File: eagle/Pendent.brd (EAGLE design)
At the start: 40.6 x 40.6 mm, 38 parts, among them Q1 CMA-4544PF-W, Q2 MPSA42, Q3 8/16/20MHz, U1 MAX9814TDFN14, U2 LF50ABDT-TR, U3 ATMEGA328

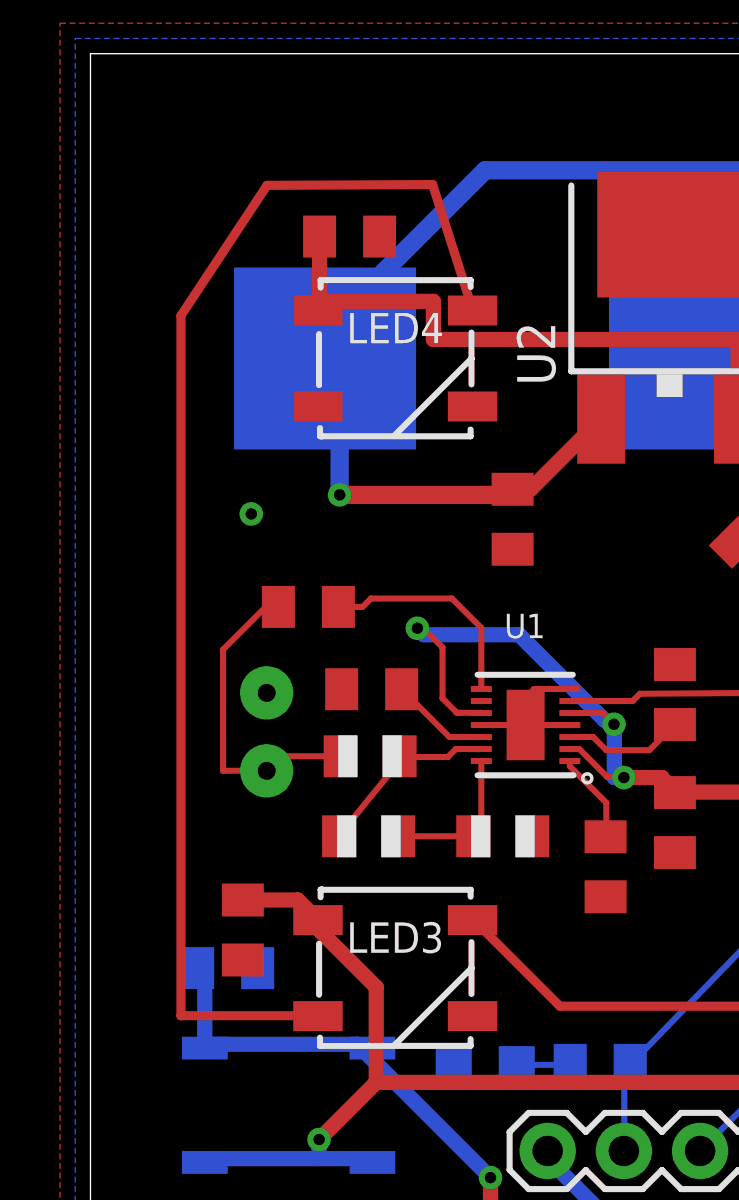
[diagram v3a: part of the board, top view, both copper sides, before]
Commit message: Add External LED Connection
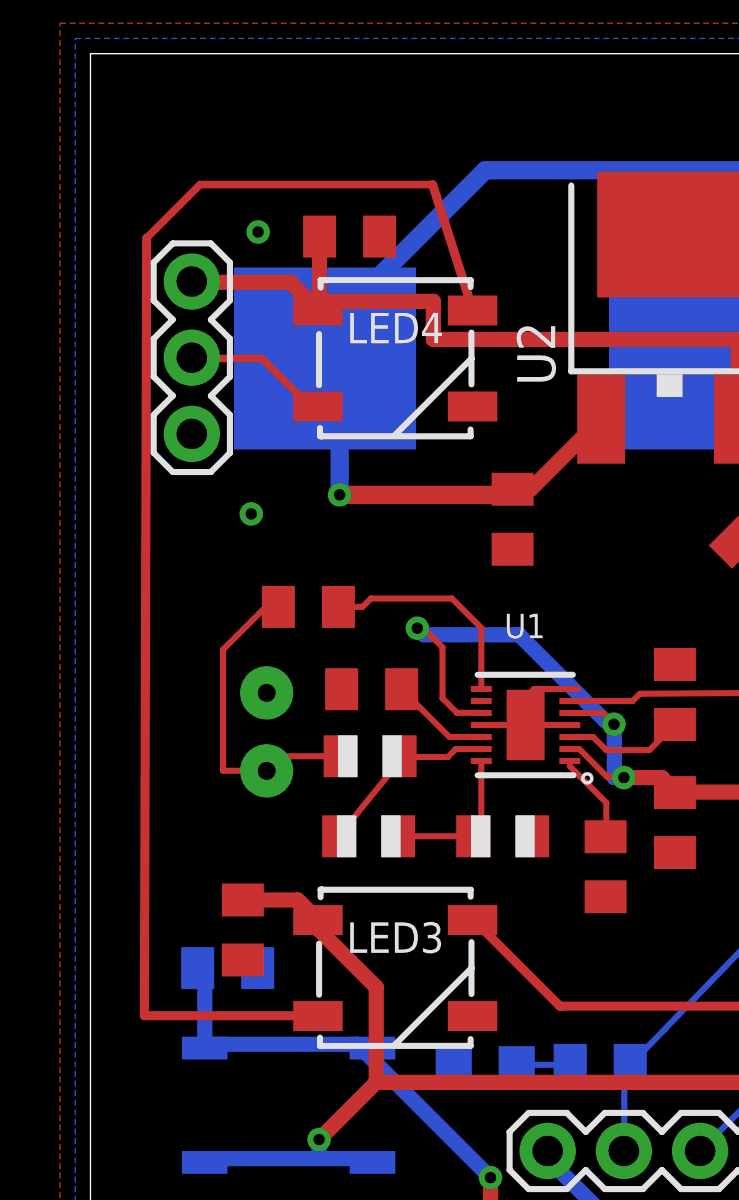
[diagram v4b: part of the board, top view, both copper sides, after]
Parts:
- added JP1: (no value), SparkFun-Connectors:1X03
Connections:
- new net N$6: JP1.2, LED4.2
- net GND: now also JP1.1
- net VCC: now also JP1.3
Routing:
- net N$6: track 0.00 -> 4.87 mm
- net VCC: track 175.1 -> 179.7 mm
- net N$3: track 43.0 -> 46.4 mm
- net GND: vias 5 -> 6
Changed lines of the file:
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@@
 <grid distance="0.1" unitdist="inch" unit="inch" style="lines" multiple="1" display="yes" altdistance="0.001" altunitdist="inch" altunit="inch"/>
 <layers>
-<layer number="1" name="Top" color="4" fill="1" visible="no" active="yes"/>
-<layer number="16" name="Bottom" color="1" fill="1" visible="no" active="yes"/>
+<layer number="1" name="Top" color="4" fill="1" visible="yes" active="yes"/>
+<layer number="16" name="Bottom" color="1" fill="1" visible="yes" active="yes"/>
 <layer number="17" name="Pads" color="2" fill="1" visible="yes" active="yes"/>
 <layer number="18" name="Vias" color="2" fill="1" visible="yes" active="yes"/>
@@
 <layer number="20" name="Dimension" color="15" fill="1" visible="yes" active="yes"/>
 <layer number="21" name="tPlace" color="7" fill="1" visible="yes" active="yes"/>
-<layer number="22" name="bPlace" color="7" fill="1" visible="no" active="yes"/>
+<layer number="22" name="bPlace" color="7" fill="1" visible="yes" active="yes"/>
 <layer number="23" name="tOrigins" color="15" fill="1" visible="yes" active="yes"/>
-<layer number="24" name="bOrigins" color="15" fill="1" visible="no" active="yes"/>
+<layer number="24" name="bOrigins" color="15" fill="1" visible="yes" active="yes"/>
 <layer number="25" name="tNames" color="7" fill="1" visible="yes" active="yes"/>
-<layer number="26" name="bNames" color="7" fill="1" visible="no" active="yes"/>
+<layer number="26" name="bNames" color="7" fill="1" visible="yes" active="yes"/>
 <layer number="27" name="tValues" color="7" fill="1" visible="yes" active="yes"/>
-<layer number="28" name="bValues" color="7" fill="1" visible="no" active="yes"/>
+<layer number="28" name="bValues" color="7" fill="1" visible="yes" active="yes"/>
 <layer number="29" name="tStop" color="7" fill="3" visible="yes" active="yes"/>
-<layer number="30" name="bStop" color="7" fill="6" visible="no" active="yes"/>
+<layer number="30" name="bStop" color="7" fill="6" visible="yes" active="yes"/>
 <layer number="31" name="tCream" color="7" fill="4" visible="yes" active="yes"/>
-<layer number="32" name="bCream" color="7" fill="5" visible="no" active="yes"/>
+<layer number="32" name="bCream" color="7" fill="5" visible="yes" active="yes"/>
 <layer number="33" name="tFinish" color="6" fill="3" visible="yes" active="yes"/>
-<layer number="34" name="bFinish" color="6" fill="6" visible="no" active="yes"/>
+<layer number="34" name="bFinish" color="6" fill="6" visible="yes" active="yes"/>
 <layer number="35" name="tGlue" color="7" fill="4" visible="yes" active="yes"/>
-<layer number="36" name="bGlue" color="7" fill="5" visible="no" active="yes"/>
+<layer number="36" name="bGlue" color="7" fill="5" visible="yes" active="yes"/>
 <layer number="37" name="tTest" color="7" fill="1" visible="yes" active="yes"/>
-<layer number="38" name="bTest" color="7" fill="1" visible="no" active="yes"/>
+<layer number="38" name="bTest" color="7" fill="1" visible="yes" active="yes"/>
 <layer number="39" name="tKeepout" color="4" fill="11" visible="yes" active="yes"/>
-<layer number="40" name="bKeepout" color="1" fill="11" visible="no" active="yes"/>
+<layer number="40" name="bKeepout" color="1" fill="11" visible="yes" active="yes"/>
 <layer number="41" name="tRestrict" color="4" fill="10" visible="yes" active="yes"/>
-<layer number="42" name="bRestrict" color="1" fill="10" visible="no" active="yes"/>
-<layer number="43" name="vRestrict" color="2" fill="10" visible="no" active="yes"/>
+<layer number="42" name="bRestrict" color="1" fill="10" visible="yes" active="yes"/>
+<layer number="43" name="vRestrict" color="2" fill="10" visible="yes" active="yes"/>
 <layer number="44" name="Drills" color="7" fill="1" visible="yes" active="yes"/>
 <layer number="45" name="Holes" color="7" fill="1" visible="yes" active="yes"/>
@@
 <layer number="49" name="Reference" color="7" fill="1" visible="yes" active="yes"/>
 <layer number="50" name="dxf" color="7" fill="1" visible="no" active="no"/>
-<layer number="51" name="tDocu" color="7" fill="1" visible="no" active="yes"/>
+<layer number="51" name="tDocu" color="7" fill="1" visible="yes" active="yes"/>
 <layer number="52" name="bDocu" color="7" fill="1" visible="yes" active="yes"/>
 <layer number="53" name="tGND_GNDA" color="7" fill="9" visible="no" active="no"/>
@@
 <text x="24.1554" y="1.4224" size="0.8128" layer="27">GND</text>
 <text x="29.0576" y="22.7838" size="0.8128" layer="52" rot="MR135">RESET</text>
+<text x="1.8542" y="26.8478" size="0.762" layer="27" rot="R90">GND</text>
 </plain>
 <attributes>
@@
 <attribute name="VALUE" x="39.2811" y="14.1605" size="0.8128" layer="27" rot="R90"/>
 </element>
+<element name="JP1" library="SparkFun-Connectors" package="1X03" value="" x="3.3782" y="27.9654" smashed="yes" rot="R90">
+<attribute name="VALUE" x="6.5532" y="26.6954" size="1.27" layer="27" rot="R90"/>
+</element>
 </elements>
 <signals>
@@
 <contactref element="C9" pad="1"/>
 <contactref element="C5" pad="1"/>
-<contactref element="LED4" pad="1"/>
 <contactref element="C2" pad="1"/>
 <contactref element="LED1" pad="1"/>
@@
 <wire x1="6.913" y1="12.43" x2="7.583" y2="11.76" width="0.508" layer="1"/>
 <wire x1="7.636" y1="34.544" x2="7.636" y2="32.133" width="0.508" layer="1"/>
-<wire x1="7.636" y1="32.133" x2="7.583" y2="32.08" width="0.508" layer="1"/>
 <wire x1="27.956" y1="34.544" x2="27.956" y2="32.133" width="0.508" layer="1"/>
 <wire x1="27.956" y1="32.133" x2="27.903" y2="32.08" width="0.508" layer="1"/>
@@
 <wire x1="21.59" y1="31.115" x2="11.43" y2="31.115" width="0.508" layer="1"/>
 <wire x1="21.59" y1="28.575" x2="21.59" y2="31.115" width="0.508" layer="1"/>
-<wire x1="7.62" y1="32.385" x2="7.583" y2="32.08" width="0.508" layer="1"/>
 <wire x1="21.59" y1="28.575" x2="21.584" y2="28.472" width="0.508" layer="1"/>
 <wire x1="9.525" y1="9.525" x2="7.62" y2="11.43" width="0.508" layer="1"/>
@@
 <wire x1="32.812053125" y1="19.05" x2="31.75" y2="19.05" width="0.508" layer="1"/>
 <wire x1="31.75" y1="19.05" x2="31.115" y2="18.415" width="0.508" layer="1"/>
+<contactref element="LED4" pad="1"/>
+<contactref element="JP1" pad="3"/>
+<wire x1="7.62" y1="32.0675" x2="7.583" y2="32.08" width="0.508" layer="1"/>
+<wire x1="7.62" y1="32.0675" x2="7.636" y2="32.133" width="0.508" layer="1"/>
+<wire x1="7.62" y1="32.385" x2="7.583" y2="32.08" width="0.508" layer="1"/>
+<wire x1="6.6675" y1="33.02" x2="7.3025" y2="32.385" width="0.508" layer="1"/>
+<wire x1="3.4925" y1="33.02" x2="6.6675" y2="33.02" width="0.508" layer="1"/>
+<wire x1="7.3025" y1="32.385" x2="7.583" y2="32.08" width="0.508" layer="1"/>
+<wire x1="3.4925" y1="33.02" x2="3.3782" y2="33.0454" width="0.508" layer="1"/>
 </signal>
 <signal name="GND">
@@
 <via x="35.1536" y="35.0012" extent="1-16" drill="0.381"/>
 <via x="35.5346" y="23.5712" extent="1-16" drill="0.381"/>
+<contactref element="JP1" pad="1"/>
+<via x="5.588" y="34.6964" extent="1-16" drill="0.381"/>
 </signal>
 <signal name="VBATT">
@@
 <contactref element="LED4" pad="4"/>
 <contactref element="LED3" pad="2"/>
-<wire x1="3.01625" y1="8.5725" x2="7.46125" y2="8.5725" width="0.3048" layer="1"/>
-<wire x1="3.01625" y1="31.90875" x2="3.01625" y2="8.5725" width="0.3048" layer="1"/>
-<wire x1="5.88645" y1="36.25215" x2="3.01625" y2="31.90875" width="0.3048" layer="1"/>
-<wire x1="11.4046" y1="36.27755" x2="5.88645" y2="36.25215" width="0.3048" layer="1"/>
+<wire x1="1.79705" y1="8.5725" x2="7.46125" y2="8.5725" width="0.3048" layer="1"/>
+<wire x1="1.87325" y1="34.49955" x2="1.79705" y2="8.5725" width="0.3048" layer="1"/>
 <wire x1="12.7" y1="32.22625" x2="11.4046" y2="36.27755" width="0.3048" layer="1"/>
 <wire x1="7.46125" y1="8.5725" x2="7.583" y2="8.56" width="0.508" layer="1"/>
 <wire x1="12.7" y1="32.22625" x2="12.737" y2="32.08" width="0.508" layer="1"/>
+<wire x1="1.87325" y1="34.49955" x2="3.65125" y2="36.27755" width="0.254" layer="1"/>
+<wire x1="3.65125" y1="36.27755" x2="11.4046" y2="36.27755" width="0.254" layer="1"/>
 </signal>
 <signal name="N$2">
@@
 <signal name="N$14">
 </signal>
+<signal name="N$6">
+<contactref element="LED4" pad="2"/>
+<contactref element="JP1" pad="2"/>
+<wire x1="5.715" y1="30.48" x2="7.3025" y2="28.8925" width="0.254" layer="1"/>
+<wire x1="3.4925" y1="30.48" x2="5.715" y2="30.48" width="0.254" layer="1"/>
+<wire x1="7.3025" y1="28.8925" x2="7.583" y2="28.88" width="0.508" layer="1"/>
+<wire x1="3.4925" y1="30.48" x2="3.3782" y2="30.5054" width="0.508" layer="1"/>
+</signal>
 </signals>

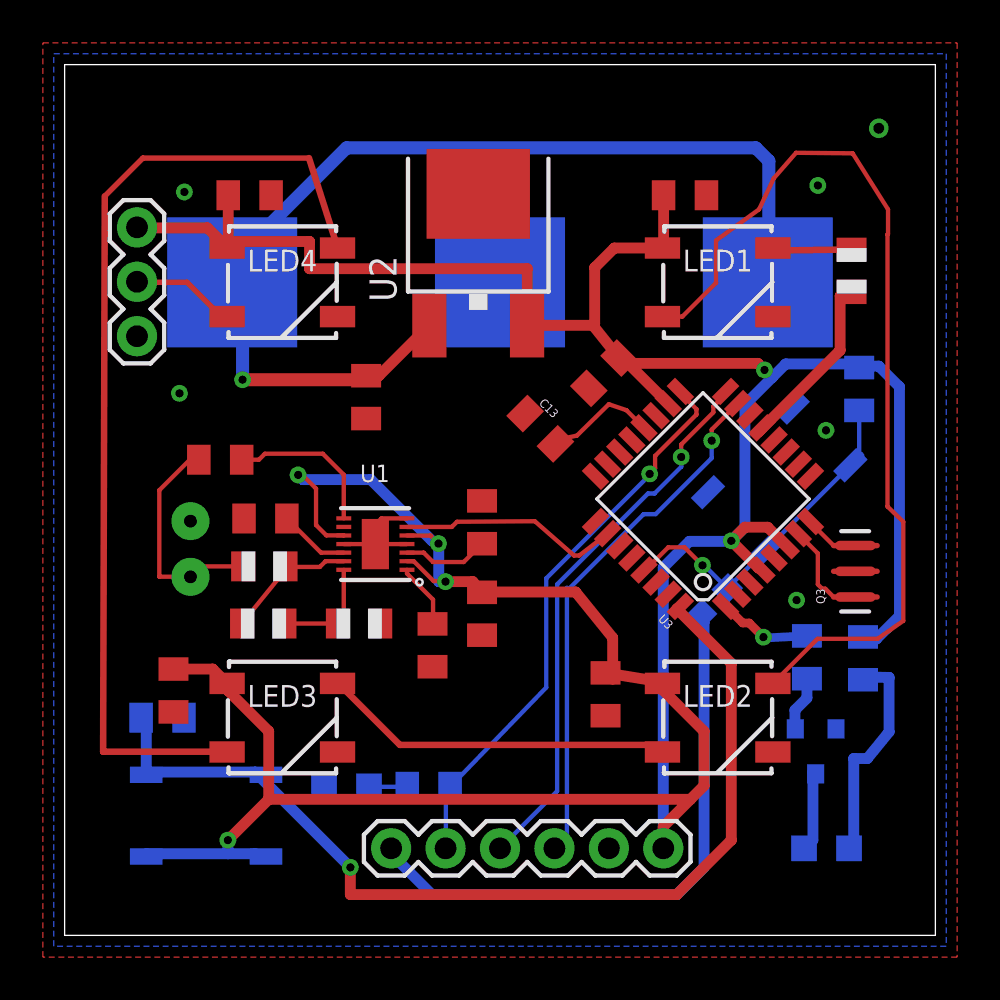
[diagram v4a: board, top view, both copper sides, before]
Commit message: Switch to correct battery footprint, switch to V13 isp
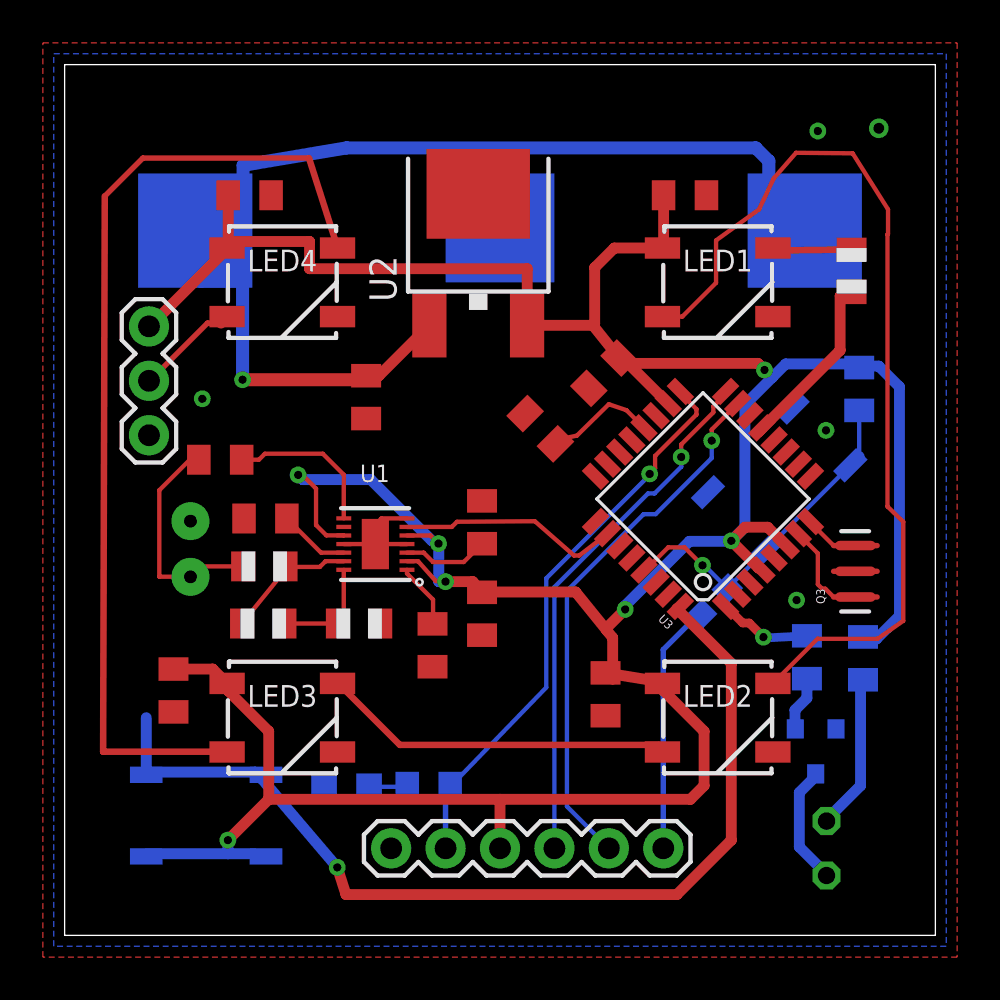
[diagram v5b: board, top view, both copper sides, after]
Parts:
- removed R4: 10k, adafruit:R0805
- LED5: device adafruit:CHIP-LED0805 -> led:LED5MM
- U$3: device SparkFun-Electromechanical:BATTCON_20MM -> bag_eagle_lib:BH2X-2032-SM
- moved JP10 12.7 mm to (27.9, 4.06), turned to 180 degrees
- moved JP1 4.66 mm to (3.94, 23.3)
- moved U$3 2.54 mm to (20.3, 33.0)
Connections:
- net D2: no longer R4.2
- net GND: now also JP10.6, S1.3, S1.4, U$3.GND; no longer JP10.5, R4.1, U$3.2
- net MOSI: now also JP10.2; no longer JP10.4
- net N$15: now also LED5.K; no longer LED5.C
- net SCK: now also JP10.5; no longer JP10.2
- net VBATT: now also U$3.P$1, U$3.P$2; no longer U$3.1
- net VCC: now also JP10.4; no longer JP10.6, S1.3, S1.4
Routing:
- net RST: track 28.0 -> 11.7 mm
- net VCC: track 179.7 -> 170.1 mm, vias 6 -> 7
- net VBATT: track 48.2 -> 57.5 mm
- net N$16: track 11.1 -> 7.29 mm
- net N$15: track 3.89 -> 5.56 mm
- net MISO: track 25.9 -> 24.8 mm
- net D2: track 46.9 -> 46.3 mm
- net GND: vias 6 -> 5
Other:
- board text added: "DAT"

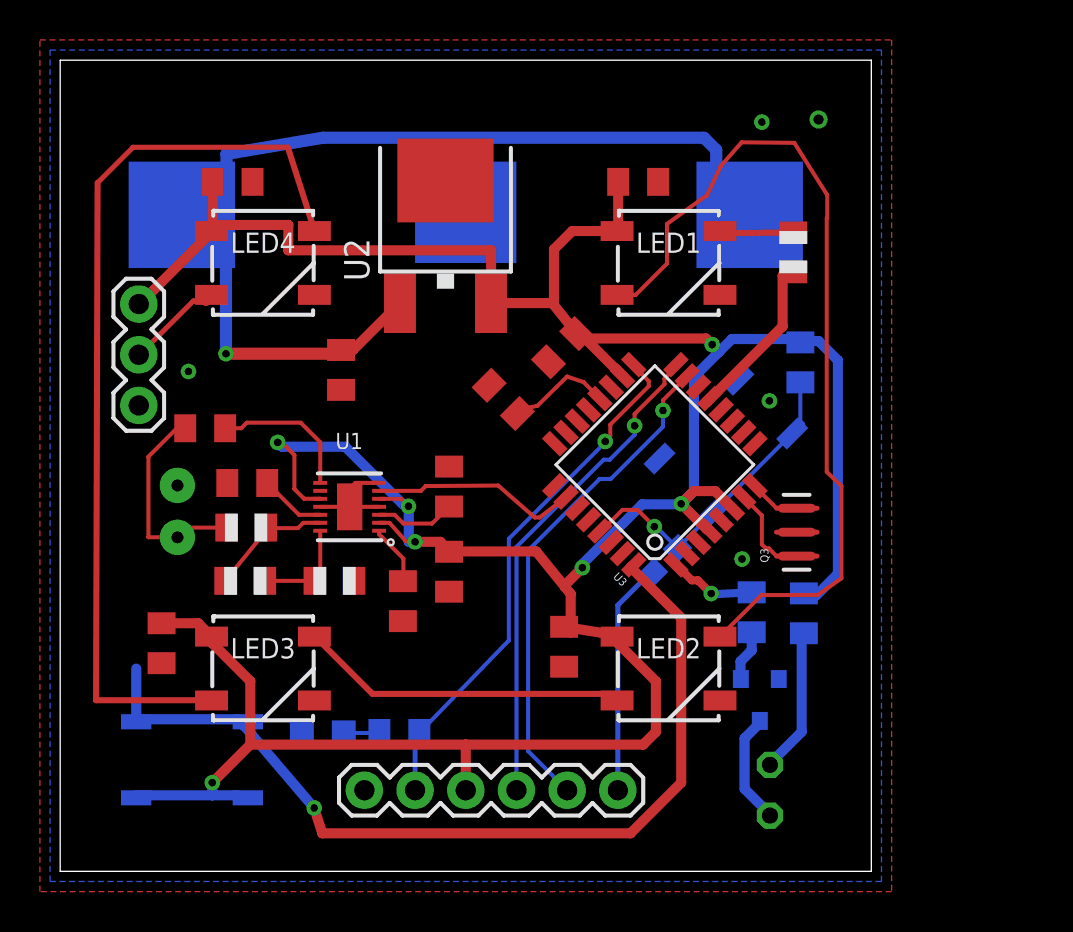
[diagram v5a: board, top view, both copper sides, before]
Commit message: Add IR Receiver
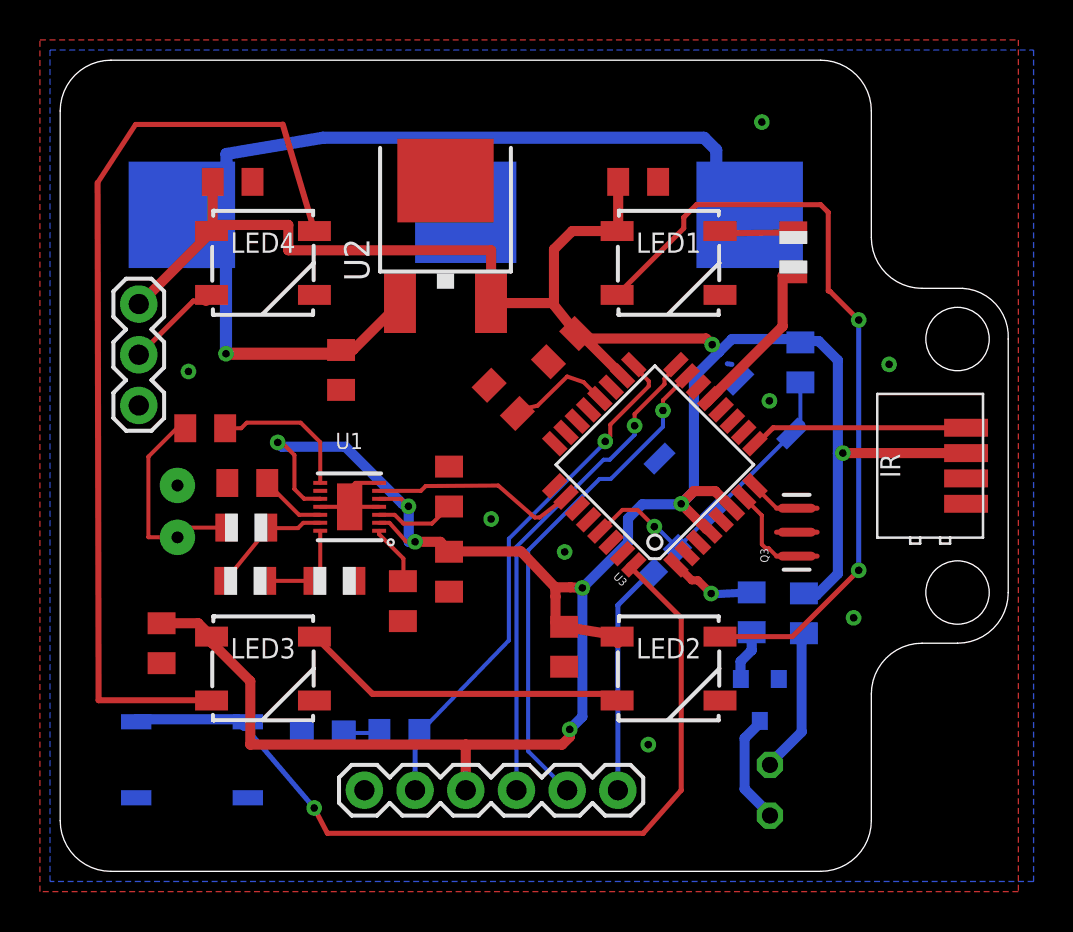
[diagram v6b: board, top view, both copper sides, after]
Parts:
- added IR: IR_TOSP6238TTCT-ND, bg_eagle_lib:TOSP62XX_A
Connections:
- net D5: now also IR.P4
- net GND: now also IR.P1
- net VCC: now also IR.P3
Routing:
- net D5: track 0.00 -> 10.9 mm
- net VCC: track 170.1 -> 166.1 mm, vias 7 -> 8
- net N$22: track 43.3 -> 40.0 mm, vias 0 -> 2
- net D2: track 46.3 -> 43.9 mm
- net N$3: track 46.4 -> 48.0 mm
- net GND: track 5.46 -> 5.69 mm, vias 5 -> 8
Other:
- board size 40.6 x 40.6 mm -> 47.5 x 40.6 mm
